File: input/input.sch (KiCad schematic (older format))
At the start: 0 parts

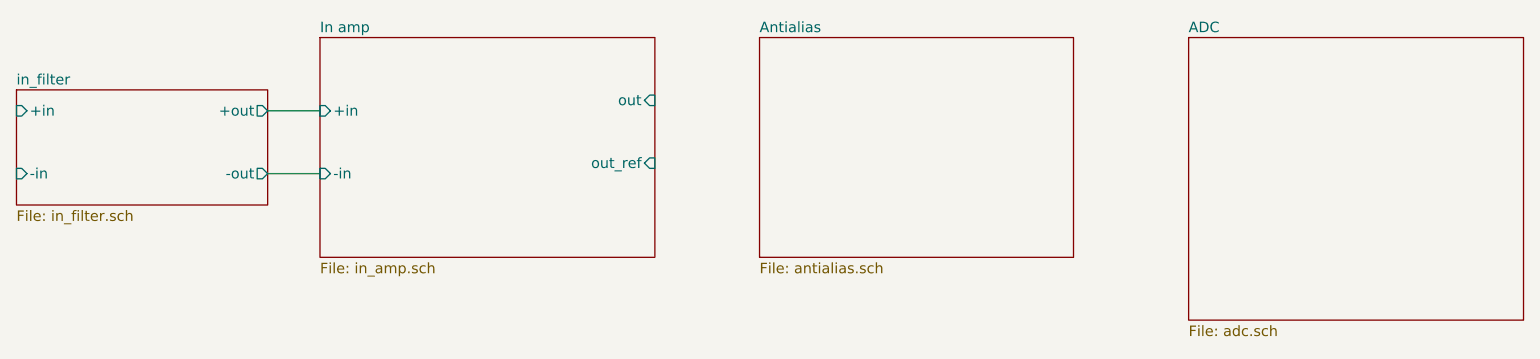
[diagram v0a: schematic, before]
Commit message: Work on schematics for antialias_driver.sch and in_filter.sch.  Spice simulations of antialias filter and reference driver.
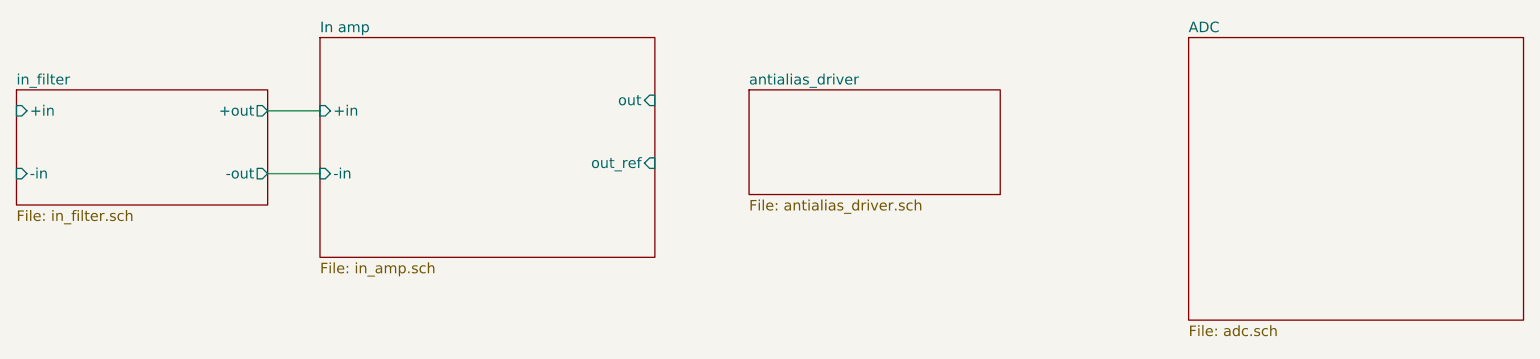
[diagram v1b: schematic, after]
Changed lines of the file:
@@
 EESchema Schematic File Version 4
 LIBS:input-cache
+LIBS:in_amp-cache
 EELAYER 29 0
 EELAYER END
@@
 F0 "ADC" 50
 F1 "adc.sch" 50
-$EndSheet
-$Sheet
-S 5500 3000 1500 1050
-U 5DA78B4D
-F0 "Antialias" 50
-F1 "antialias.sch" 50
 $EndSheet
 $Sheet
@@
 Wire Wire Line
 	3150 3650 3400 3650
+$Sheet
+S 5450 3250 1200 500
+U 5DE6CDF8
+F0 "antialias_driver" 50
+F1 "antialias_driver.sch" 50
+$EndSheet
 $EndSCHEMATC
